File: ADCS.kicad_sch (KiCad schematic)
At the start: 14 parts

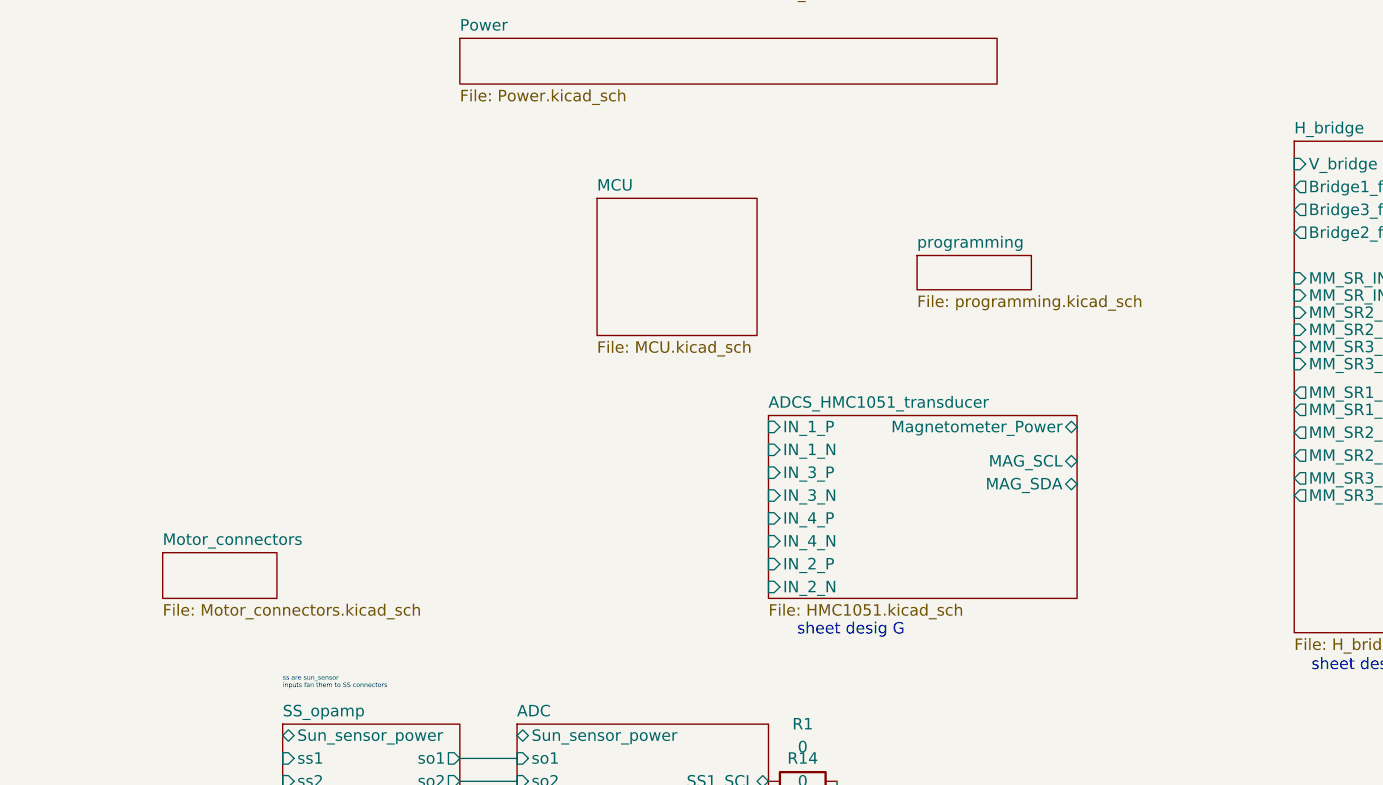
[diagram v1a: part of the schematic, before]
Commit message: add power and processor and connectors
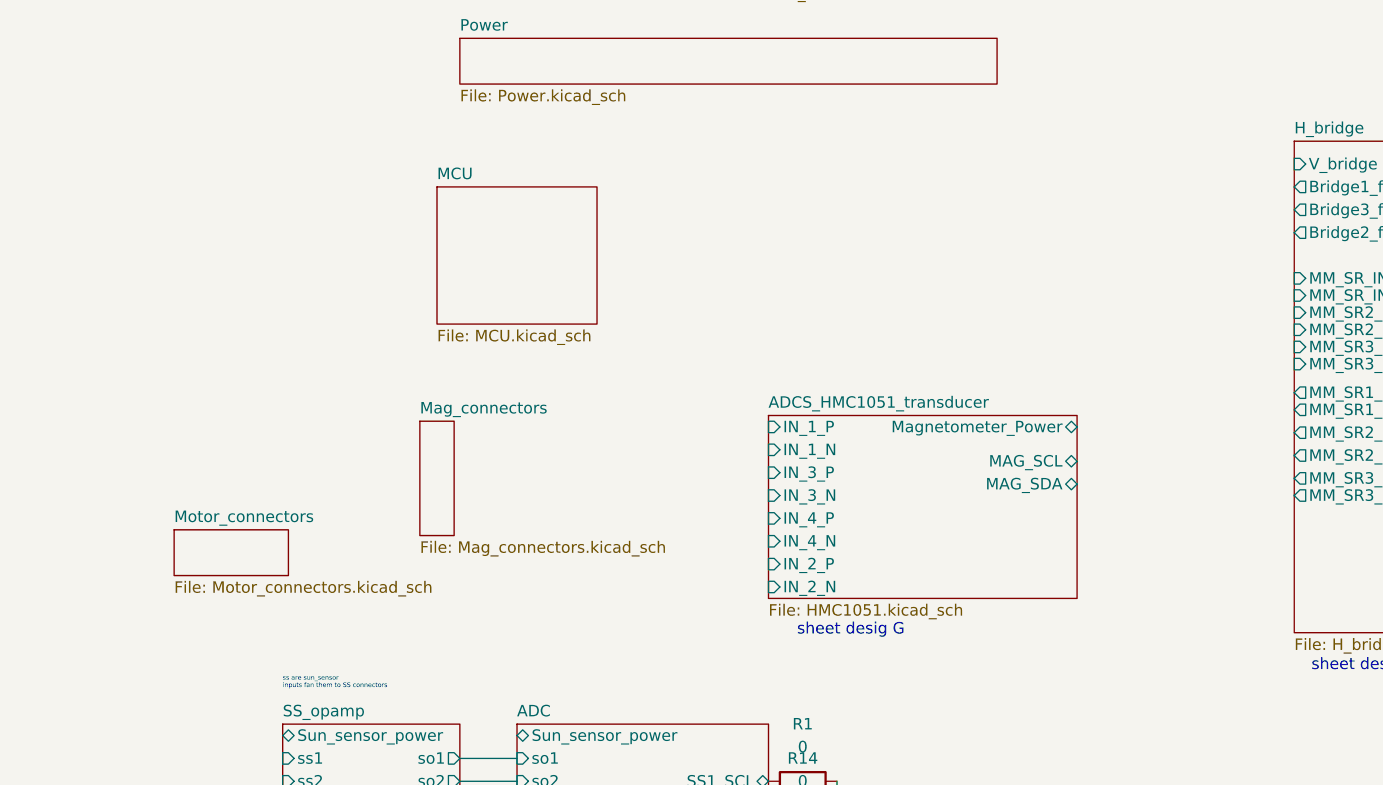
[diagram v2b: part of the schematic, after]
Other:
- removed sheet programming
- added sheet Mag_connectors (Mag_connectors.kicad_sch)
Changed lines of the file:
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@@
     (pin "2")
   )
-  (sheet (at 121.92 48.26) (size 17.78 15.24) (fields_autoplaced)
+  (sheet (at 104.14 46.99) (size 17.78 15.24) (fields_autoplaced)
     (stroke (width 0.1524) (type solid) (color 0 0 0 0))
     (fill (color 0 0 0 0.0000))
-    (property "Sheet name" "MCU" (id 0) (at 121.92 47.5484 0)
-      (effects (font (size 1.27 1.27)) (justify left bottom))
-    )
-    (property "Sheet file" "MCU.kicad_sch" (id 1) (at 121.92 64.0846 0)
-      (effects (font (size 1.27 1.27)) (justify left top))
-    )
-  )
-  (sheet (at 73.66 87.63) (size 12.7 5.08) (fields_autoplaced)
+    (property "Sheet name" "MCU" (id 0) (at 104.14 46.2784 0)
+      (effects (font (size 1.27 1.27)) (justify left bottom))
+    )
+    (property "Sheet file" "MCU.kicad_sch" (id 1) (at 104.14 62.8146 0)
+      (effects (font (size 1.27 1.27)) (justify left top))
+    )
+  )
+  (sheet (at 74.93 85.09) (size 12.7 5.08) (fields_autoplaced)
     (stroke (width 0.1524) (type solid) (color 0 0 0 0))
     (fill (color 0 0 0 0.0000))
-    (property "Sheet name" "Motor_connectors" (id 0) (at 73.66 86.9184 0)
-      (effects (font (size 1.27 1.27)) (justify left bottom))
-    )
-    (property "Sheet file" "Motor_connectors.kicad_sch" (id 1) (at 73.66 93.2946 0)
+    (property "Sheet name" "Motor_connectors" (id 0) (at 74.93 84.3784 0)
+      (effects (font (size 1.27 1.27)) (justify left bottom))
+    )
+    (property "Sheet file" "Motor_connectors.kicad_sch" (id 1) (at 74.93 90.7546 0)
       (effects (font (size 1.27 1.27)) (justify left top))
     )
@@
     )
   )
+  (sheet (at 102.235 73.025) (size 3.81 12.7) (fields_autoplaced)
+    (stroke (width 0.1524) (type solid) (color 0 0 0 0))
+    (fill (color 0 0 0 0.0000))
+    (property "Sheet name" "Mag_connectors" (id 0) (at 102.235 72.3134 0)
+      (effects (font (size 1.27 1.27)) (justify left bottom))
+    )
+    (property "Sheet file" "Mag_connectors.kicad_sch" (id 1) (at 102.235 86.3096 0)
+      (effects (font (size 1.27 1.27)) (justify left top))
+    )
+  )
   (sheet (at 140.97 72.39) (size 34.29 20.32) (fields_autoplaced)
     (stroke (width 0.1524) (type solid) (color 255 46 44 1))
@@
     (pin "IN_2_N" input (at 140.97 91.44 180)
       (effects (font (size 1.27 1.27)) (justify left))
-    )
-  )
-  (sheet (at 157.48 54.61) (size 12.7 3.81) (fields_autoplaced)
-    (stroke (width 0.1524) (type solid) (color 0 0 0 0))
-    (fill (color 0 0 0 0.0000))
-    (property "Sheet name" "programming" (id 0) (at 157.48 53.8984 0)
-      (effects (font (size 1.27 1.27)) (justify left bottom))
-    )
-    (property "Sheet file" "programming.kicad_sch" (id 1) (at 157.48 59.0046 0)
-      (effects (font (size 1.27 1.27)) (justify left top))
     )
   )
@@
     (path "/6e8df492-8c59-43fd-94ed-550a415f346a" (page "13"))
     (path "/4d1fba12-6ef0-42d4-9064-f9f362dde9b9" (page "14"))
+    (path "/90eea1cc-3897-47cb-b6ba-95228c17b7e0" (page "15"))
     (path "/8fa611b7-cf75-4378-bd5d-72096b0e3078" (page "15"))
-    (path "/bfb5174f-75b4-4de7-8dcd-166ce97a61ad" (page "15"))
   )
   (symbol_instances
@@
     )
     (path "/e17995dd-10f0-48f3-8f39-76f49c739fd3/ff3be686-81d4-4575-9ed4-6dfbe71c9e5e"
-      (reference "CH1") (unit 1) (value "C") (footprint "")
+      (reference "CH1") (unit 1) (value "0.01u") (footprint "")
     )
     (path "/e17995dd-10f0-48f3-8f39-76f49c739fd3/47666723-7086-4ebc-972d-c8e3c4484282"
@@
     )
     (path "/e17995dd-10f0-48f3-8f39-76f49c739fd3/3d12bbc4-9b26-4015-b2d4-260cbbfdf537"
-      (reference "CH9") (unit 1) (value "C") (footprint "")
+      (reference "CH9") (unit 1) (value "0.01u") (footprint "")
     )
     (path "/e17995dd-10f0-48f3-8f39-76f49c739fd3/059bbcee-27cf-4da8-a0a2-ab467b4ebc46"
@@
     )
     (path "/e17995dd-10f0-48f3-8f39-76f49c739fd3/0e4dc100-1ace-405c-86cd-663b446e8f15"
-      (reference "CH11") (unit 1) (value "C") (footprint "")
+      (reference "CH11") (unit 1) (value "10u") (footprint "")
     )
     (path "/e17995dd-10f0-48f3-8f39-76f49c739fd3/8d00b2b9-ffc0-4200-bdd0-cc0ba84197bc"
-      (reference "CH12") (unit 1) (value "C") (footprint "")
+      (reference "CH12") (unit 1) (value "2.2u") (footprint "")
     )
     (path "/e17995dd-10f0-48f3-8f39-76f49c739fd3/d1e06862-e80d-4203-8ad4-d4e5d2f2a4bf"
@@
     )
     (path "/e17995dd-10f0-48f3-8f39-76f49c739fd3/15369ae3-b7e8-4b9e-ad97-b758e025dd04"
-      (reference "CH15") (unit 1) (value "C") (footprint "")
+      (reference "CH15") (unit 1) (value "0.01u") (footprint "")
     )
     (path "/e17995dd-10f0-48f3-8f39-76f49c739fd3/99ca94b0-0e04-47a0-bc9f-49f0cbc12487"
@@
     )
     (path "/e17995dd-10f0-48f3-8f39-76f49c739fd3/6edc97e2-1a4e-452a-a611-945f6942da06"
-      (reference "CH17") (unit 1) (value "C") (footprint "")
+      (reference "CH17") (unit 1) (value "10u") (footprint "")
     )
     (path "/e17995dd-10f0-48f3-8f39-76f49c739fd3/79021f8d-f911-4f3e-9a8d-ef5d710af21d"
-      (reference "CH18") (unit 1) (value "C") (footprint "")
+      (reference "CH18") (unit 1) (value "2.2u") (footprint "")
     )
     (path "/bada602b-dbd3-4fb8-afdd-ed6e71e7ad90/cdb6aa5c-566b-4f24-9679-f7b1e64ed563"

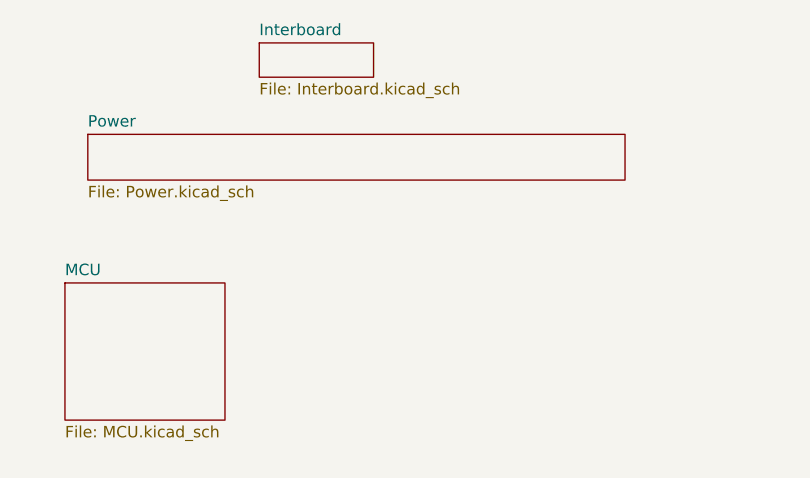
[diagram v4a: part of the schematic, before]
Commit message: MCU_pinout_except_timer please add connector symbols and footprint folder, i will send you parts throughout the day
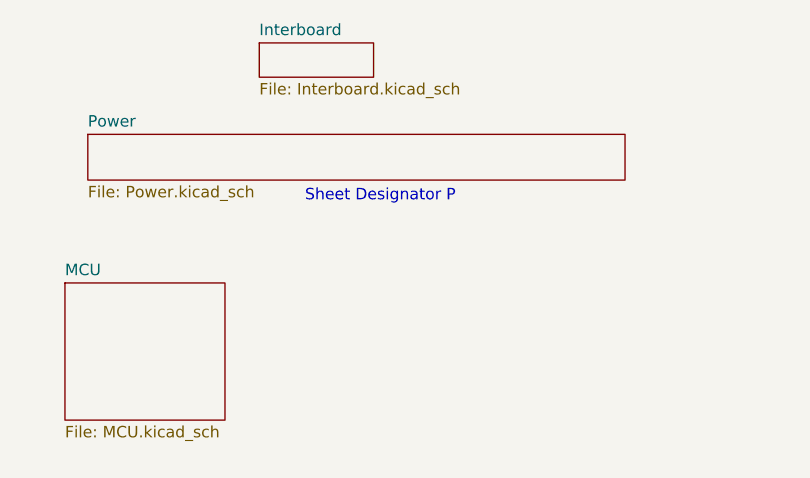
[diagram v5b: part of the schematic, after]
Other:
- note added: "Sheet Designator P"
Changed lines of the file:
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@@
+    (effects (font (size 1.27 1.27)) (justify left bottom))
+  )
+  (text "Sheet Designator P\n" (at 130.81 38.1 0)
     (effects (font (size 1.27 1.27)) (justify left bottom))
   )
@@
       (reference "#PWR?") (unit 1) (value "GND") (footprint "")
     )
-    (path "/fb0a46e4-ada8-472b-b73c-3a0177e61b01/9a0f6c97-0c31-4bdf-bb83-c3d5bd89bcc0"
-      (reference "?") (unit 1) (value "ST1S06PUR") (footprint "")
+    (path "/212d50e9-da32-4d3f-8d53-7380f45f0f28/5630ecd1-dbbf-4934-9622-ce986f087d53"
+      (reference "?") (unit 1) (value "STM32H725ZGT6") (footprint "")
     )
     (path "/bada602b-dbd3-4fb8-afdd-ed6e71e7ad90/09e9f576-75ea-4b13-ba60-52e7e8cae27e"
@@
       (reference "U?") (unit 1) (value "LMV324") (footprint "")
     )
-    (path "/fb0a46e4-ada8-472b-b73c-3a0177e61b01/9739f66c-15bd-4223-81a5-022506570f50"
-      (reference "U?") (unit 1) (value "ST1S06PUR") (footprint "")
-    )
     (path "/ea192a91-d6b2-496f-9935-87312cd8ef80/a404ecd4-24bf-4c96-ba6a-960ad63ea2b7"
       (reference "U?") (unit 1) (value "LMV324") (footprint "")
     )
-    (path "/fb0a46e4-ada8-472b-b73c-3a0177e61b01/ba4fcbb1-6c4f-485a-9a4e-51f5811dfe32"
-      (reference "U?") (unit 1) (value "L7983PUR") (footprint "")
-    )
     (path "/ea192a91-d6b2-496f-9935-87312cd8ef80/c9ab5a20-c8a2-4a41-ad2a-8c8b2c875d7c"
       (reference "U?") (unit 1) (value "LMV324") (footprint "")
@@
       (reference "UH3") (unit 1) (value "DRV8833PWP") (footprint "Package_SO:HTSSOP-16-1EP_4.4x5mm_P0.65mm_EP3.4x5mm_Mask2.46x2.31mm_ThermalVias")
     )
-  )
+    (path "/fb0a46e4-ada8-472b-b73c-3a0177e61b01/ba4fcbb1-6c4f-485a-9a4e-51f5811dfe32"
+      (reference "UP1") (unit 1) (value "L7983PUR") (footprint "")
+    )
+    (path "/fb0a46e4-ada8-472b-b73c-3a0177e61b01/9a0f6c97-0c31-4bdf-bb83-c3d5bd89bcc0"
+      (reference "UP2") (unit 1) (value "ST1S06PUR") (footprint "")
+    )
+    (path "/fb0a46e4-ada8-472b-b73c-3a0177e61b01/9739f66c-15bd-4223-81a5-022506570f50"
+      (reference "UP3") (unit 1) (value "ST1S06PUR") (footprint "")
+    )
+  )

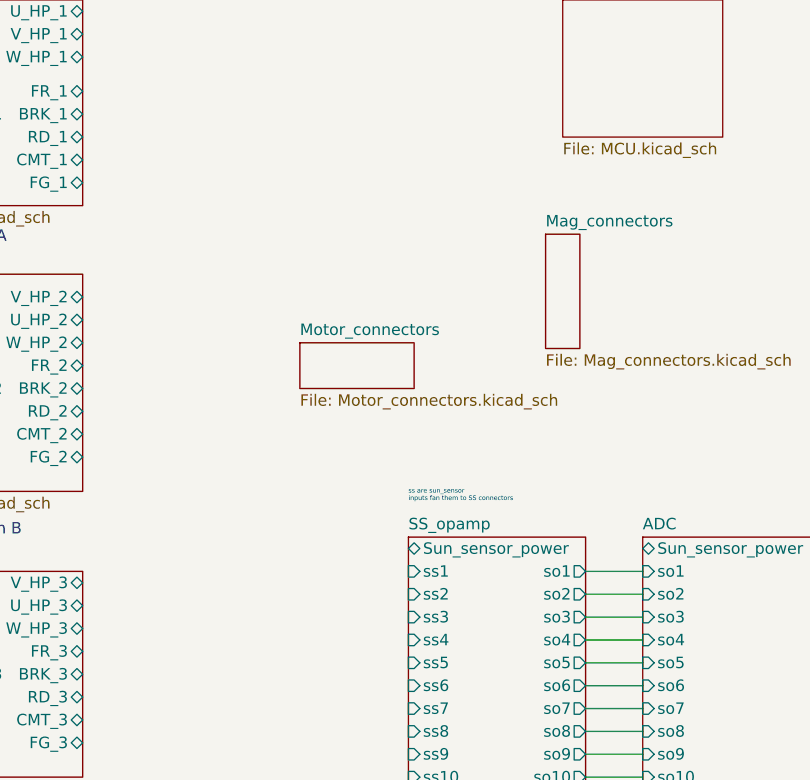
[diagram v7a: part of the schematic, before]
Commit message: Motor connectors added check pinout with motor wiring
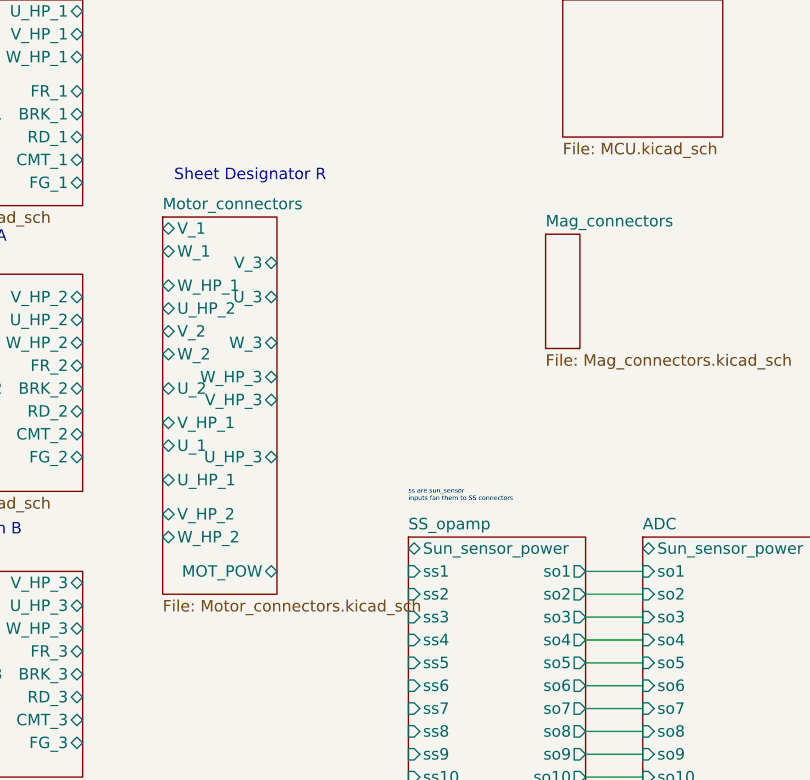
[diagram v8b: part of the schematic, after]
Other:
- sheet Motor_connectors ports: added MOT_POW, U_1, U_2, U_3, U_HP_1, U_HP_2, U_HP_3, V_1, V_2, V_3, V_HP_1, V_HP_2, V_HP_3, W_1, W_2, W_3, W_HP_1, W_HP_2, W_HP_3; removed none
- note added: "Sheet Designator R"
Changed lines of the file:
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@@
+    (effects (font (size 1.27 1.27)) (justify left bottom))
+  )
+  (text "Sheet Designator R\n" (at 60.96 67.31 0)
     (effects (font (size 1.27 1.27)) (justify left bottom))
   )
@@
     )
   )
-  (sheet (at 74.93 85.09) (size 12.7 5.08) (fields_autoplaced)
+  (sheet (at 59.69 71.12) (size 12.7 41.91) (fields_autoplaced)
     (stroke (width 0.1524) (type solid) (color 0 0 0 0))
     (fill (color 0 0 0 0.0000))
-    (property "Sheet name" "Motor_connectors" (id 0) (at 74.93 84.3784 0)
+    (property "Sheet name" "Motor_connectors" (id 0) (at 59.69 70.4084 0)
       (effects (font (size 1.27 1.27)) (justify left bottom))
     )
-    (property "Sheet file" "Motor_connectors.kicad_sch" (id 1) (at 74.93 90.7546 0)
+    (property "Sheet file" "Motor_connectors.kicad_sch" (id 1) (at 59.69 113.6146 0)
       (effects (font (size 1.27 1.27)) (justify left top))
+    )
+    (pin "V_1" bidirectional (at 59.69 72.39 180)
+      (effects (font (size 1.27 1.27)) (justify left))
+    )
+    (pin "MOT_POW" bidirectional (at 72.39 110.49 0)
+      (effects (font (size 1.27 1.27)) (justify right))
+    )
+    (pin "W_1" bidirectional (at 59.69 74.93 180)
+      (effects (font (size 1.27 1.27)) (justify left))
+    )
+    (pin "W_HP_1" bidirectional (at 59.69 78.74 180)
+      (effects (font (size 1.27 1.27)) (justify left))
+    )
+    (pin "U_HP_2" bidirectional (at 59.69 81.28 180)
+      (effects (font (size 1.27 1.27)) (justify left))
+    )
+    (pin "V_2" bidirectional (at 59.69 83.82 180)
+      (effects (font (size 1.27 1.27)) (justify left))
+    )
+    (pin "W_2" bidirectional (at 59.69 86.36 180)
+      (effects (font (size 1.27 1.27)) (justify left))
+    )
+    (pin "U_2" bidirectional (at 59.69 90.17 180)
+      (effects (font (size 1.27 1.27)) (justify left))
+    )
+    (pin "V_HP_1" bidirectional (at 59.69 93.98 180)
+      (effects (font (size 1.27 1.27)) (justify left))
+    )
+    (pin "U_1" bidirectional (at 59.69 96.52 180)
+      (effects (font (size 1.27 1.27)) (justify left))
+    )
+    (pin "U_HP_1" bidirectional (at 59.69 100.33 180)
+      (effects (font (size 1.27 1.27)) (justify left))
+    )
+    (pin "V_HP_2" bidirectional (at 59.69 104.14 180)
+      (effects (font (size 1.27 1.27)) (justify left))
+    )
+    (pin "W_HP_2" bidirectional (at 59.69 106.68 180)
+      (effects (font (size 1.27 1.27)) (justify left))
+    )
+    (pin "V_3" bidirectional (at 72.39 76.2 0)
+      (effects (font (size 1.27 1.27)) (justify right))
+    )
+    (pin "W_3" bidirectional (at 72.39 85.09 0)
+      (effects (font (size 1.27 1.27)) (justify right))
+    )
+    (pin "V_HP_3" bidirectional (at 72.39 91.44 0)
+      (effects (font (size 1.27 1.27)) (justify right))
+    )
+    (pin "U_HP_3" bidirectional (at 72.39 97.79 0)
+      (effects (font (size 1.27 1.27)) (justify right))
+    )
+    (pin "U_3" bidirectional (at 72.39 80.01 0)
+      (effects (font (size 1.27 1.27)) (justify right))
+    )
+    (pin "W_HP_3" bidirectional (at 72.39 88.9 0)
+      (effects (font (size 1.27 1.27)) (justify right))
     )
   )
@@
       (reference "#PWR0235") (unit 1) (value "GND") (footprint "")
     )
+    (path "/4c63012e-f7ed-4767-81b5-36fd3817b900/2d5c5ceb-06f5-4883-a5ec-e3e8242e2aba"
+      (reference "#PWR?") (unit 1) (value "GND") (footprint "")
+    )
+    (path "/4c63012e-f7ed-4767-81b5-36fd3817b900/35279086-bb3c-4960-a980-9d69ab0a3d1f"
+      (reference "#PWR?") (unit 1) (value "GND") (footprint "")
+    )
+    (path "/4c63012e-f7ed-4767-81b5-36fd3817b900/552d4df4-e0dd-4bad-8581-6d4b2be314c4"
+      (reference "#PWR?") (unit 1) (value "GND") (footprint "")
+    )
+    (path "/4c63012e-f7ed-4767-81b5-36fd3817b900/89971111-60b1-47e3-bbdf-0eab108b6b1f"
+      (reference "#PWR?") (unit 1) (value "GND") (footprint "")
+    )
     (path "/212d50e9-da32-4d3f-8d53-7380f45f0f28/a02550f7-5d68-4f7f-af17-7aa7f6409e6f"
       (reference "#PWR?") (unit 1) (value "GND") (footprint "")
     )
+    (path "/4c63012e-f7ed-4767-81b5-36fd3817b900/bec4dba5-de6f-4c84-883f-6a54226c6d11"
+      (reference "#PWR?") (unit 1) (value "GND") (footprint "")
+    )
+    (path "/4c63012e-f7ed-4767-81b5-36fd3817b900/c6477b01-1185-4e9a-9595-289e6114ee75"
+      (reference "#PWR?") (unit 1) (value "GND") (footprint "")
+    )
     (path "/212d50e9-da32-4d3f-8d53-7380f45f0f28/fea6d1c0-dee6-47b2-b0b8-fa7833396fbd"
       (reference "#PWR?") (unit 1) (value "GND") (footprint "")
@@
       (reference "UP3") (unit 1) (value "ST1S06PUR") (footprint "ST1S06PUR:SON95P300X300X100-7N-D")
     )
+    (path "/4c63012e-f7ed-4767-81b5-36fd3817b900/1caa193f-47a9-4707-8ff6-e547ac843a06"
+      (reference "UR1") (unit 1) (value "2367196-8") (footprint "")
+    )
+    (path "/4c63012e-f7ed-4767-81b5-36fd3817b900/e29971db-0454-483c-96db-b5f54309795e"
+      (reference "UR2") (unit 1) (value "2367196-8") (footprint "")
+    )
+    (path "/4c63012e-f7ed-4767-81b5-36fd3817b900/be901eba-16e1-4ad1-9f39-a9f4d29032b2"
+      (reference "UR3") (unit 1) (value "2367196-8") (footprint "")
+    )
     (path "/212d50e9-da32-4d3f-8d53-7380f45f0f28/4f23dd0a-4038-463c-9342-6978adc78155"
